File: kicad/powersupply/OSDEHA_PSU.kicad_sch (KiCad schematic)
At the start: 56 parts, among them J1 340 VAC / 220 mA, J2 340 VAC / 220 mA, J3 420 VAC / 75 mA, J4 9 VAC / 4.5 A, J5 Stator bias, J6 HV-L, J7 HV-R, J8 HEATERS-LEFT, J9 HEATERS-RIGHT, K1 RT424006, Q1 BD138, Q2 10M90S, U1 LM1085-ADJ, U2 NE555P

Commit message: up
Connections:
- net HV_STABI1/AC1: now also J1.2 (Pin_2); no longer J1.1 (Pin_1)
- net HV_STABI1/AC2: now also K1.21; no longer K1.11
- net HV_STABI2/AC1: now also J2.1 (Pin_1); no longer J2.2 (Pin_2)
- net HV_STABI2/AC2: now also K1.11; no longer K1.21
- net at K1.14: now also J2.2 (Pin_2); no longer J1.2 (Pin_2)
- net at K1.24: now also J1.1 (Pin_1); no longer J2.1 (Pin_1)
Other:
- note added: "Heater and buffer+gridbias supply turn on first B+ and B- turn on with delay"
- note removed: "Filament, heater and buffer+gridbias supply turn on first B+ and B- turn on with delay"

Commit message: psu pcb
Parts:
- R11: footprint Resistor_THT:R_Axial_DIN0207_L6.3mm_D2.5mm_P10.16mm_Horizontal -> Resistor_THT:R_Axial_DIN0207_L6.3mm_D2.5mm_P2.54mm_Vertical
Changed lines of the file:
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@@
       (effects (font (size 1.27 1.27)))
     )
-    (property "Footprint" "Resistor_THT:R_Axial_DIN0207_L6.3mm_D2.5mm_P10.16mm_Horizontal" (at 148.59 62.992 90)
+    (property "Footprint" "Resistor_THT:R_Axial_DIN0207_L6.3mm_D2.5mm_P2.54mm_Vertical" (at 148.59 62.992 90)
       (effects (font (size 1.27 1.27)) hide)
     )

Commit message: psu pcb
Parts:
- R5, R6: footprint Resistor_THT:R_Axial_DIN0207_L6.3mm_D2.5mm_P10.16mm_Horizontal -> Resistor_THT:R_Axial_DIN0207_L6.3mm_D2.5mm_P2.54mm_Vertical
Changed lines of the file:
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@@
       (effects (font (size 1.27 1.27)))
     )
-    (property "Footprint" "Resistor_THT:R_Axial_DIN0207_L6.3mm_D2.5mm_P10.16mm_Horizontal" (at 106.172 60.96 90)
+    (property "Footprint" "Resistor_THT:R_Axial_DIN0207_L6.3mm_D2.5mm_P2.54mm_Vertical" (at 106.172 60.96 90)
       (effects (font (size 1.27 1.27)) hide)
     )
@@
       (effects (font (size 1.27 1.27)))
     )
-    (property "Footprint" "Resistor_THT:R_Axial_DIN0207_L6.3mm_D2.5mm_P10.16mm_Horizontal" (at 102.87 51.562 90)
+    (property "Footprint" "Resistor_THT:R_Axial_DIN0207_L6.3mm_D2.5mm_P2.54mm_Vertical" (at 102.87 51.562 90)
       (effects (font (size 1.27 1.27)) hide)
     )

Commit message: pcb psu
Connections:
- net HV_STABI3/AC1: now also J3.2 (Pin_2); no longer J3.1 (Pin_1)
- net HV_STABI3/AC2: now also J3.1 (Pin_1); no longer J3.2 (Pin_2)
- net at D2.2 (A), D4.2 (A): now also J4.1 (Pin_1); no longer J4.2 (Pin_2)
- net at D1.1 (K), D3.2 (A): now also J4.2 (Pin_2); no longer J4.1 (Pin_1)
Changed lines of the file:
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@@
-    )
-  )
-  (symbol (lib_id "Connector:Screw_Terminal_01x02") (at 38.1 222.25 0) (mirror y) (unit 1)
-    (in_bom yes) (on_board yes) (dnp no)
-    (property "Reference" "J4" (at 35.56 222.25 0)
-      (effects (font (size 1.27 1.27)) (justify left))
-    )
-    (property "Value" "9 VAC / 4.5 A" (at 35.56 224.79 0)
-      (effects (font (size 1.27 1.27)) (justify left))
-    )
-    (property "Footprint" "TerminalBlock_Phoenix:TerminalBlock_Phoenix_MKDS-1,5-2-5.08_1x02_P5.08mm_Horizontal" (at 38.1 222.25 0)
-      (effects (font (size 1.27 1.27)) hide)
-    )
-    (property "Datasheet" "https://www.phoenixcontact.com/us/products/1729128/pdf" (at 38.1 222.25 0)
-      (effects (font (size 1.27 1.27)) hide)
-    )
-    (property "MPN" "1729128 " (at 38.1 222.25 0)
-      (effects (font (size 1.27 1.27)) hide)
-    )
-    (pin "2")
-    (pin "1")
-    (instances
-      (project "OSDEHA_PSU"
-        (path "/ca37e2fa-48ac-4eb3-a7a4-1e3bbee61661"
-          (reference "J4") (unit 1)
-        )
-      )
     )
   )
@@
     )
   )
+  (symbol (lib_id "Connector:Screw_Terminal_01x02") (at 38.1 224.79 180) (unit 1)
+    (in_bom yes) (on_board yes) (dnp no)
+    (property "Reference" "J4" (at 35.56 222.25 0)
+      (effects (font (size 1.27 1.27)) (justify left))
+    )
+    (property "Value" "9 VAC / 4.5 A" (at 35.56 224.79 0)
+      (effects (font (size 1.27 1.27)) (justify left))
+    )
+    (property "Footprint" "TerminalBlock_Phoenix:TerminalBlock_Phoenix_MKDS-1,5-2-5.08_1x02_P5.08mm_Horizontal" (at 38.1 224.79 0)
+      (effects (font (size 1.27 1.27)) hide)
+    )
+    (property "Datasheet" "https://www.phoenixcontact.com/us/products/1729128/pdf" (at 38.1 224.79 0)
+      (effects (font (size 1.27 1.27)) hide)
+    )
+    (property "MPN" "1729128 " (at 38.1 224.79 0)
+      (effects (font (size 1.27 1.27)) hide)
+    )
+    (pin "2")
+    (pin "1")
+    (instances
+      (project "OSDEHA_PSU"
+        (path "/ca37e2fa-48ac-4eb3-a7a4-1e3bbee61661"
+          (reference "J4") (unit 1)
+        )
+      )
+    )
+  )
   (symbol (lib_id "Mechanical:MountingHole") (at 354.33 233.68 0) (unit 1)
     (in_bom yes) (on_board yes) (dnp no) (fields_autoplaced)
@@
     )
   )
+  (symbol (lib_id "Connector:Screw_Terminal_01x02") (at 38.1 121.92 180) (unit 1)
+    (in_bom yes) (on_board yes) (dnp no)
+    (property "Reference" "J3" (at 35.56 119.38 0)
+      (effects (font (size 1.27 1.27)) (justify left))
+    )
+    (property "Value" "420 VAC / 75 mA" (at 35.56 121.92 0)
+      (effects (font (size 1.27 1.27)) (justify left))
+    )
+    (property "Footprint" "TerminalBlock_Phoenix:TerminalBlock_Phoenix_MKDS-1,5-2-5.08_1x02_P5.08mm_Horizontal" (at 38.1 121.92 0)
+      (effects (font (size 1.27 1.27)) hide)
+    )
+    (property "Datasheet" "https://www.phoenixcontact.com/us/products/1729128/pdf" (at 38.1 121.92 0)
+      (effects (font (size 1.27 1.27)) hide)
+    )
+    (property "MPN" "1729128 " (at 38.1 121.92 0)
+      (effects (font (size 1.27 1.27)) hide)
+    )
+    (pin "2")
+    (pin "1")
+    (instances
+      (project "OSDEHA_PSU"
+        (path "/ca37e2fa-48ac-4eb3-a7a4-1e3bbee61661"
+          (reference "J3") (unit 1)
+        )
+      )
+    )
+  )
   (symbol (lib_id "power:GND") (at 200.66 68.58 0) (unit 1)
     (in_bom yes) (on_board yes) (dnp no) (fields_autoplaced)
@@
         )
       )
-    )
-  )
-  (symbol (lib_id "Connector:Screw_Terminal_01x02") (at 38.1 119.38 0) (mirror y) (unit 1)
-    (in_bom yes) (on_board yes) (dnp no)
-    (property "Reference" "J3" (at 35.56 119.38 0)
-      (effects (font (size 1.27 1.27)) (justify left))
-    )
-    (property "Value" "420 VAC / 75 mA" (at 35.56 121.92 0)
-      (effects (font (size 1.27 1.27)) (justify left))
-    )
-    (property "Footprint" "TerminalBlock_Phoenix:TerminalBlock_Phoenix_MKDS-1,5-2-5.08_1x02_P5.08mm_Horizontal" (at 38.1 119.38 0)
-      (effects (font (size 1.27 1.27)) hide)
-    )
-    (property "Datasheet" "https://www.phoenixcontact.com/us/products/1729128/pdf" (at 38.1 119.38 0)
-      (effects (font (size 1.27 1.27)) hide)
-    )
-    (property "MPN" "1729128 " (at 38.1 119.38 0)
-      (effects (font (size 1.27 1.27)) hide)
-    )
-    (pin "2")
-    (pin "1")
-    (instances
-      (project "OSDEHA_PSU"
-        (path "/ca37e2fa-48ac-4eb3-a7a4-1e3bbee61661"
-          (reference "J3") (unit 1)
-        )
-      )

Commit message: PSU PCB
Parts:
- removed H1, H2, H3: MountingHole, MountingHole:MountingHole_3.2mm_M3, symbol Mechanical:MountingHole
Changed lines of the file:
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@@
-    )
-  )
-  (symbol (lib_id "Mechanical:MountingHole") (at 354.33 228.6 0) (unit 1)
-    (in_bom yes) (on_board yes) (dnp no) (fields_autoplaced)
-    (property "Reference" "H2" (at 356.87 228.6 0)
-      (effects (font (size 1.27 1.27)) (justify left) hide)
-    )
-    (property "Value" "MountingHole" (at 356.87 229.87 0)
-      (effects (font (size 1.27 1.27)) (justify left) hide)
-    )
-    (property "Footprint" "MountingHole:MountingHole_3.2mm_M3" (at 354.33 228.6 0)
-      (effects (font (size 1.27 1.27)) hide)
-    )
-    (property "Datasheet" "~" (at 354.33 228.6 0)
-      (effects (font (size 1.27 1.27)) hide)
-    )
-    (instances
-      (project "OSDEHA_PSU"
-        (path "/ca37e2fa-48ac-4eb3-a7a4-1e3bbee61661"
-          (reference "H2") (unit 1)
-        )
-      )
     )
   )
@@
     )
   )
-  (symbol (lib_id "Mechanical:MountingHole") (at 347.98 233.68 0) (unit 1)
-    (in_bom yes) (on_board yes) (dnp no) (fields_autoplaced)
-    (property "Reference" "H1" (at 350.52 232.41 0)
-      (effects (font (size 1.27 1.27)) (justify left) hide)
-    )
-    (property "Value" "MountingHole" (at 350.52 233.68 0)
-      (effects (font (size 1.27 1.27)) (justify left) hide)
-    )
-    (property "Footprint" "MountingHole:MountingHole_3.2mm_M3" (at 347.98 233.68 0)
-      (effects (font (size 1.27 1.27)) hide)
-    )
-    (property "Datasheet" "~" (at 347.98 233.68 0)
-      (effects (font (size 1.27 1.27)) hide)
-    )
-    (instances
-      (project "OSDEHA_PSU"
-        (path "/ca37e2fa-48ac-4eb3-a7a4-1e3bbee61661"
-          (reference "H1") (unit 1)
-        )
-      )
-    )
-  )
   (symbol (lib_id "Device:R") (at 93.98 106.68 270) (unit 1)
     (in_bom yes) (on_board yes) (dnp no)
@@
         )
       )
-    )
-  )
-  (symbol (lib_id "Mechanical:MountingHole") (at 354.33 233.68 0) (unit 1)
-    (in_bom yes) (on_board yes) (dnp no) (fields_autoplaced)
-    (property "Reference" "H3" (at 356.87 232.41 0)
-      (effects (font (size 1.27 1.27)) (justify left) hide)
-    )
-    (property "Value" "MountingHole" (at 356.87 233.68 0)
-      (effects (font (size 1.27 1.27)) (justify left) hide)
-    )
-    (property "Footprint" "MountingHole:MountingHole_3.2mm_M3" (at 354.33 233.68 0)
-      (effects (font (size 1.27 1.27)) hide)
-    )
-    (property "Datasheet" "~" (at 354.33 233.68 0)
-      (effects (font (size 1.27 1.27)) hide)
-    )
-    (instances
-      (project "OSDEHA_PSU"
-        (path "/ca37e2fa-48ac-4eb3-a7a4-1e3bbee61661"
-          (reference "H3") (unit 1)
-        )
-      )

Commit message: pcb
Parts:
- added H1, H2, H3: MountingHole, MountingHole:MountingHole_3.2mm_M3, symbol Mechanical:MountingHole
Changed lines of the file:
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@@
+    )
+  )
+  (symbol (lib_id "Mechanical:MountingHole") (at 368.3 238.76 0) (unit 1)
+    (in_bom yes) (on_board yes) (dnp no) (fields_autoplaced)
+    (property "Reference" "H3" (at 370.84 237.49 0)
+      (effects (font (size 1.27 1.27)) (justify left))
+    )
+    (property "Value" "MountingHole" (at 370.84 240.03 0)
+      (effects (font (size 1.27 1.27)) (justify left))
+    )
+    (property "Footprint" "MountingHole:MountingHole_3.2mm_M3" (at 368.3 238.76 0)
+      (effects (font (size 1.27 1.27)) hide)
+    )
+    (property "Datasheet" "~" (at 368.3 238.76 0)
+      (effects (font (size 1.27 1.27)) hide)
+    )
+    (instances
+      (project "OSDEHA_PSU"
+        (path "/ca37e2fa-48ac-4eb3-a7a4-1e3bbee61661"
+          (reference "H3") (unit 1)
+        )
+      )
     )
   )
@@
     )
   )
+  (symbol (lib_id "Mechanical:MountingHole") (at 368.3 228.6 0) (unit 1)
+    (in_bom yes) (on_board yes) (dnp no) (fields_autoplaced)
+    (property "Reference" "H1" (at 370.84 227.33 0)
+      (effects (font (size 1.27 1.27)) (justify left))
+    )
+    (property "Value" "MountingHole" (at 370.84 229.87 0)
+      (effects (font (size 1.27 1.27)) (justify left))
+    )
+    (property "Footprint" "MountingHole:MountingHole_3.2mm_M3" (at 368.3 228.6 0)
+      (effects (font (size 1.27 1.27)) hide)
+    )
+    (property "Datasheet" "~" (at 368.3 228.6 0)
+      (effects (font (size 1.27 1.27)) hide)
+    )
+    (instances
+      (project "OSDEHA_PSU"
+        (path "/ca37e2fa-48ac-4eb3-a7a4-1e3bbee61661"
+          (reference "H1") (unit 1)
+        )
+      )
+    )
+  )
   (symbol (lib_id "Device:R") (at 120.65 237.49 0) (unit 1)
     (in_bom yes) (on_board yes) (dnp no)
@@
         )
       )
+    )
+  )
+  (symbol (lib_id "Mechanical:MountingHole") (at 368.3 233.68 0) (unit 1)
+    (in_bom yes) (on_board yes) (dnp no) (fields_autoplaced)
+    (property "Reference" "H2" (at 370.84 232.41 0)
+      (effects (font (size 1.27 1.27)) (justify left))
+    )
+    (property "Value" "MountingHole" (at 370.84 234.95 0)
+      (effects (font (size 1.27 1.27)) (justify left))
+    )
+    (property "Footprint" "MountingHole:MountingHole_3.2mm_M3" (at 368.3 233.68 0)
+      (effects (font (size 1.27 1.27)) hide)
+    )
+    (property "Datasheet" "~" (at 368.3 233.68 0)
+      (effects (font (size 1.27 1.27)) hide)
+    )
+    (instances
+      (project "OSDEHA_PSU"
+        (path "/ca37e2fa-48ac-4eb3-a7a4-1e3bbee61661"
+          (reference "H2") (unit 1)
+        )
+      )

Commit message: parts
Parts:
- C7: MPN 860160372003 -> 860160372003
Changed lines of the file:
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@@
       (effects (font (size 1.27 1.27)) hide)
     )
-    (property "MPN" "860160372003 " (at 137.16 232.41 90)
+    (property "MPN" "860160372003" (at 137.16 232.41 90)
       (effects (font (size 1.27 1.27)) hide)
     )

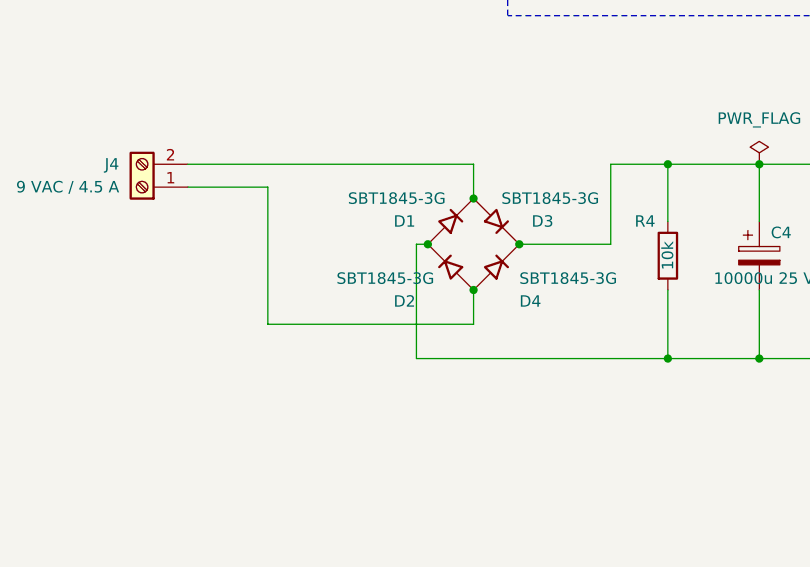
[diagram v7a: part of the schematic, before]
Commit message: fix polarity of D2
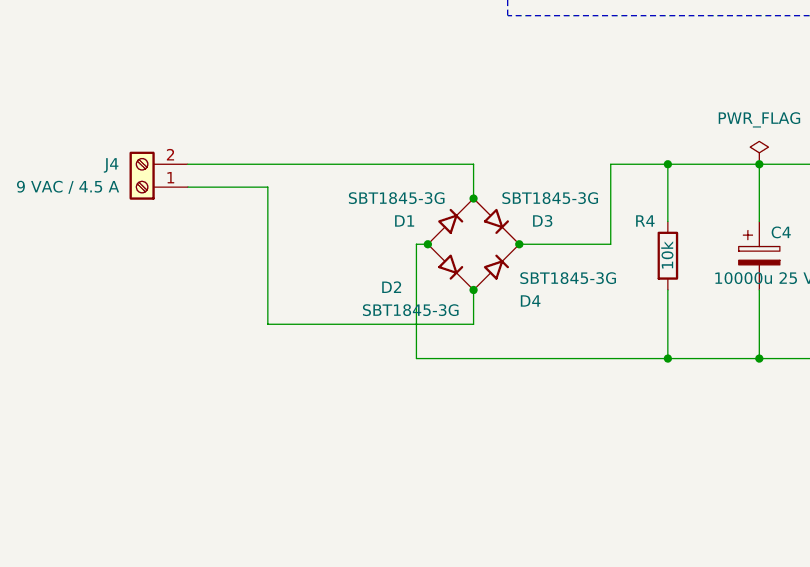
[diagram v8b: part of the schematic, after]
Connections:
- net GND: now also D2.2 (A); no longer D2.1 (K)
- net at D4.2 (A), J4.1 (Pin_1): now also D2.1 (K); no longer D2.2 (A)
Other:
- moved on the sheet: D2
